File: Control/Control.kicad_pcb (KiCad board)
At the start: 2 copper layers, 157.5 x 90.2 mm, 56 parts, among them J1 Conn_01x04_Pin, J2 Conn_01x08_Pin, J3 Conn_01x08_Pin, J4 Conn_01x07_Pin, SW1 SW_MEC_5E, U1 AT28C64B-15PI, U2 AT28C64B-15PI, U3 SN74AC14N, U4 SN74AC14N, U5 74LS163, U6 74HCT138, U7 74HCT00

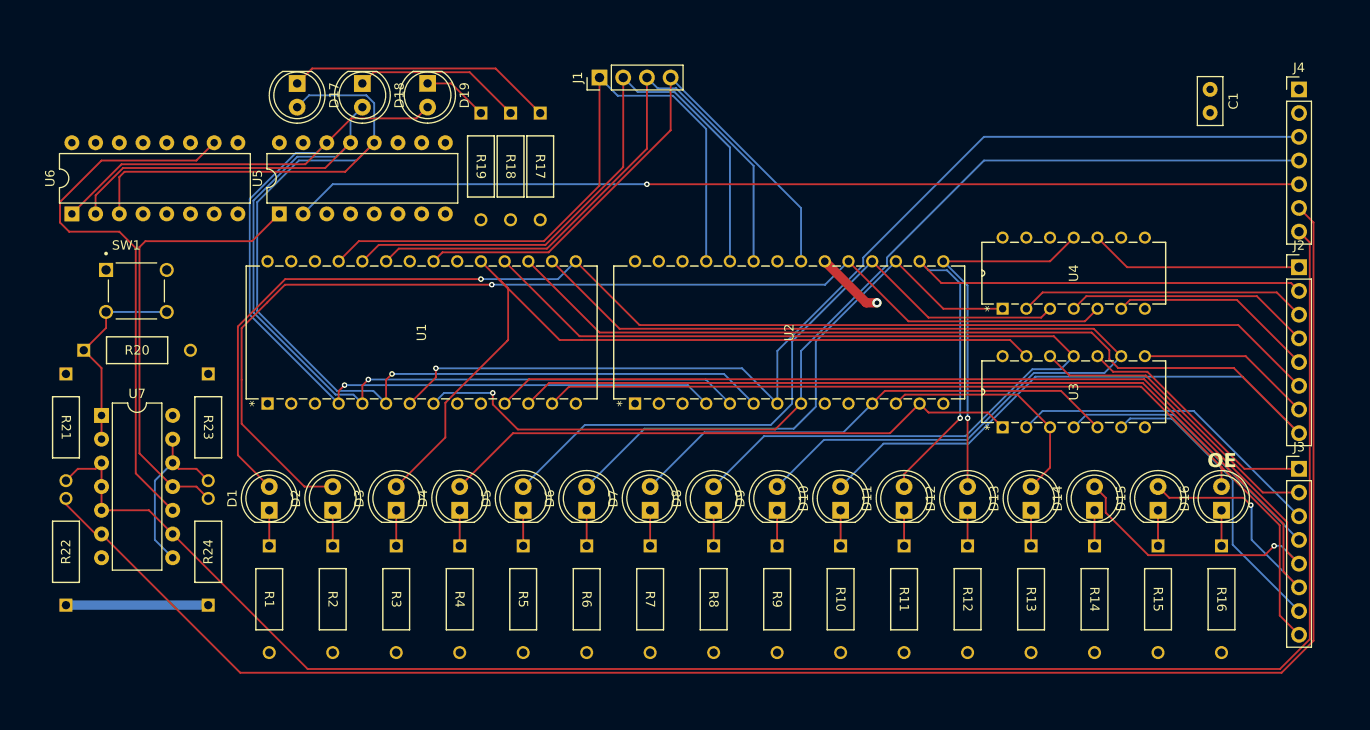
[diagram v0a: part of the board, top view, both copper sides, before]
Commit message: Added silkscreen labels to control LEDs. And other minor silkscreen updates
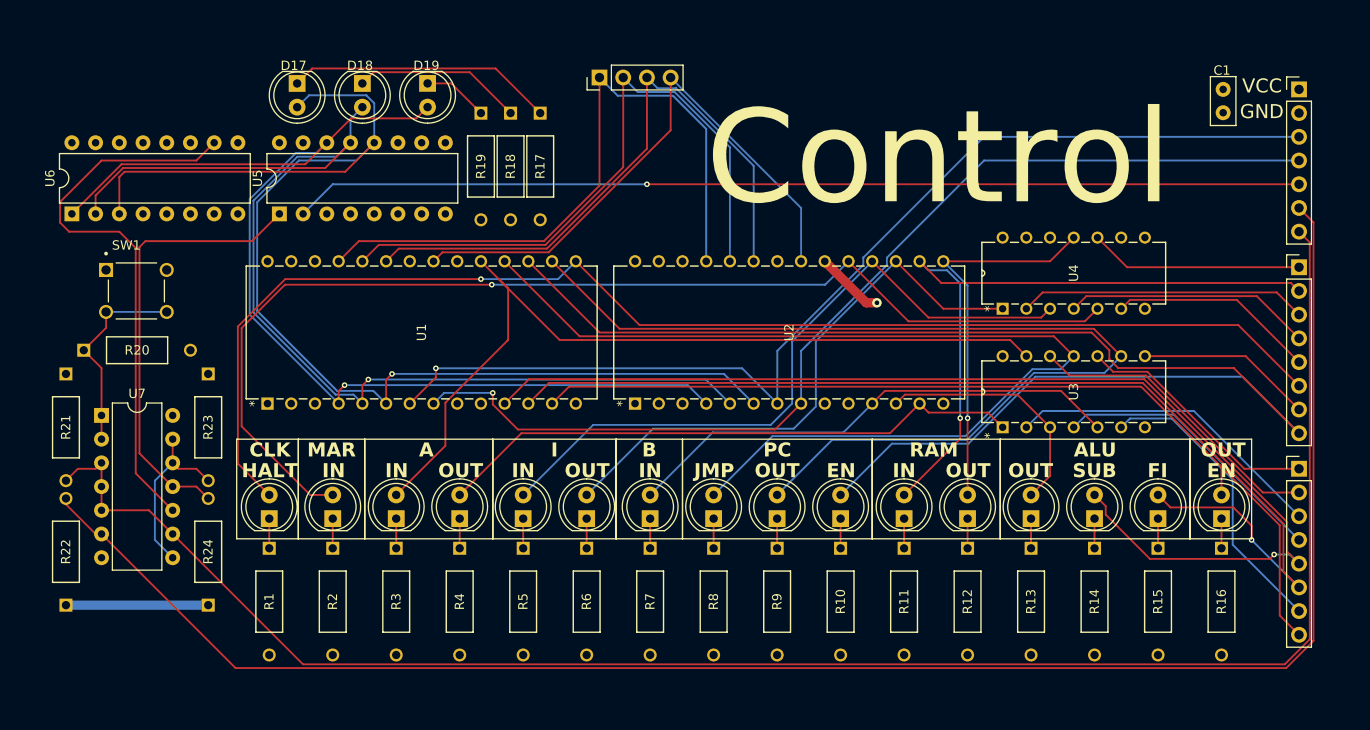
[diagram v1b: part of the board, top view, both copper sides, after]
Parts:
- moved C1 1.40 mm to (182.4, 86.4)
- moved D1 0.89 mm to (80.2, 132.3)
- moved D10 0.89 mm to (141.4, 132.3)
- moved D11 0.89 mm to (148.2, 132.3)
- moved D12 0.89 mm to (155.0, 132.3)
- moved D13 0.89 mm to (161.8, 132.3)
- moved D14 0.89 mm to (168.6, 132.3)
- moved D15 0.89 mm to (175.4, 132.3)
- moved D16 0.89 mm to (182.2, 132.3)
- moved D2 0.89 mm to (87.0, 132.3)
- moved D3 0.89 mm to (93.8, 132.3)
- moved D4 0.89 mm to (100.6, 132.3)
- moved D5 0.89 mm to (107.4, 132.3)
- moved D6 0.89 mm to (114.2, 132.3)
- moved D7 0.89 mm to (121.0, 132.3)
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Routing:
- net /ALU_FLAGS_IN: track 117.3 -> 115.6 mm
- net /ALU_SUB: track 123.3 -> 122.1 mm
- net /Output_EN: track 99.8 -> 100.7 mm
- net /RAM_WO: track 40.2 -> 41.1 mm
- net /RAM_RI: track 71.5 -> 72.4 mm
- net /CLK_Halt: track 140.6 -> 141.5 mm
- net /AR_RI: track 90.2 -> 91.1 mm
- net /ALU_WRITE: track 25.6 -> 26.4 mm
- net Net-(D9-K): track 3.81 -> 3.18 mm
- net Net-(D8-K): track 3.81 -> 3.18 mm
- net Net-(D7-K): track 3.81 -> 3.18 mm
- net Net-(D6-K): track 3.81 -> 3.18 mm
- net Net-(D5-K): track 3.81 -> 3.18 mm
- net Net-(D4-K): track 3.81 -> 3.18 mm
- net Net-(D3-K): track 3.81 -> 3.18 mm
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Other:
- board text added: "A"
- board text added: "ALU"
- board text added: "B"
- board text added: "CLK"
- board text added: "Control"
- board text added: "EN"
- board text added: "FI"
- board text added: "GND"
- board text added: "HALT"
- board text added: "I"
- board text added: "IN"
- board text added: "JMP"
- board text added: "MAR"
- board text added: "OUT"
- board text added: "PC"
- board text added: "RAM"
- board text added: "SUB"
- board text added: "VCC"
- board text removed: "OE"

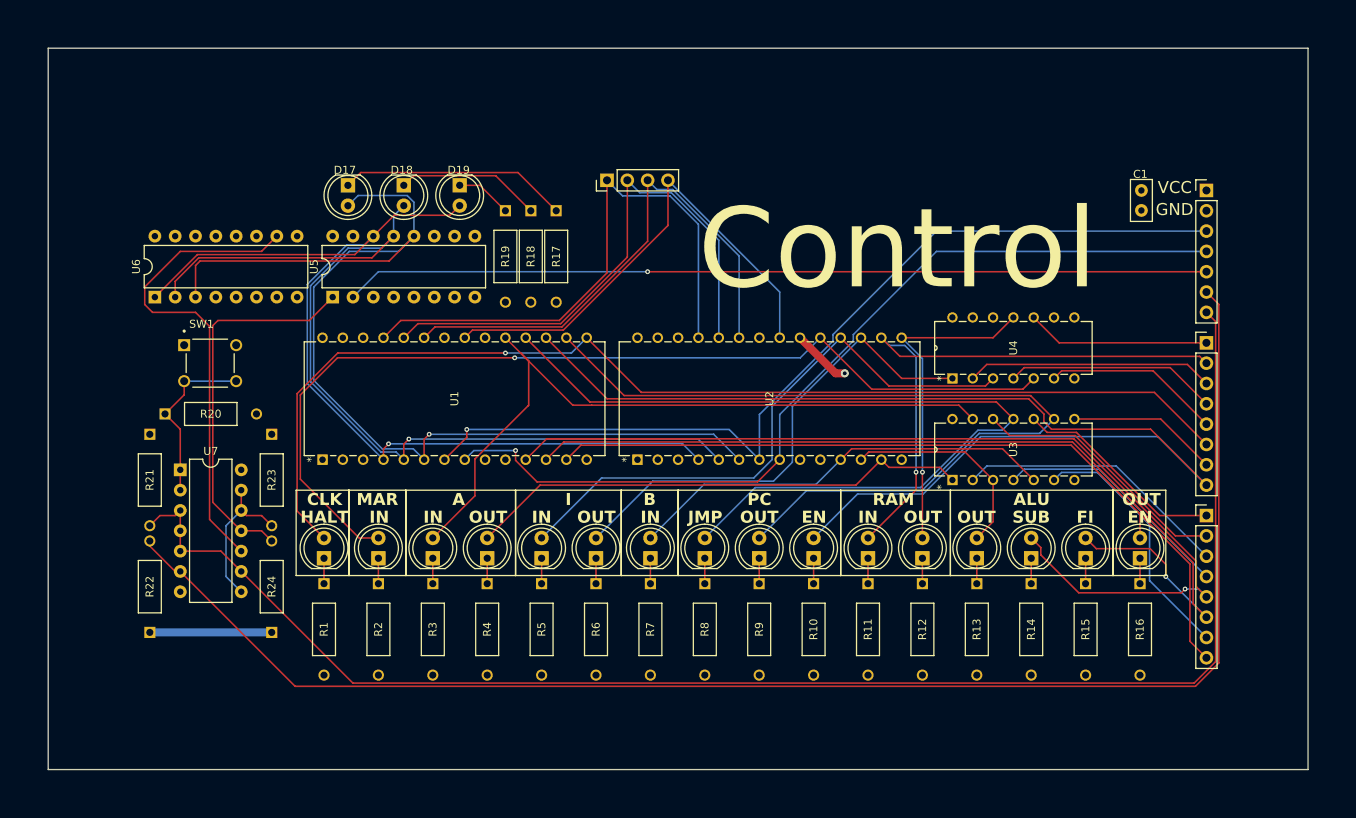
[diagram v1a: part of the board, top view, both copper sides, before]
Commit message: Added edge cuts and mounting holes to control PCB
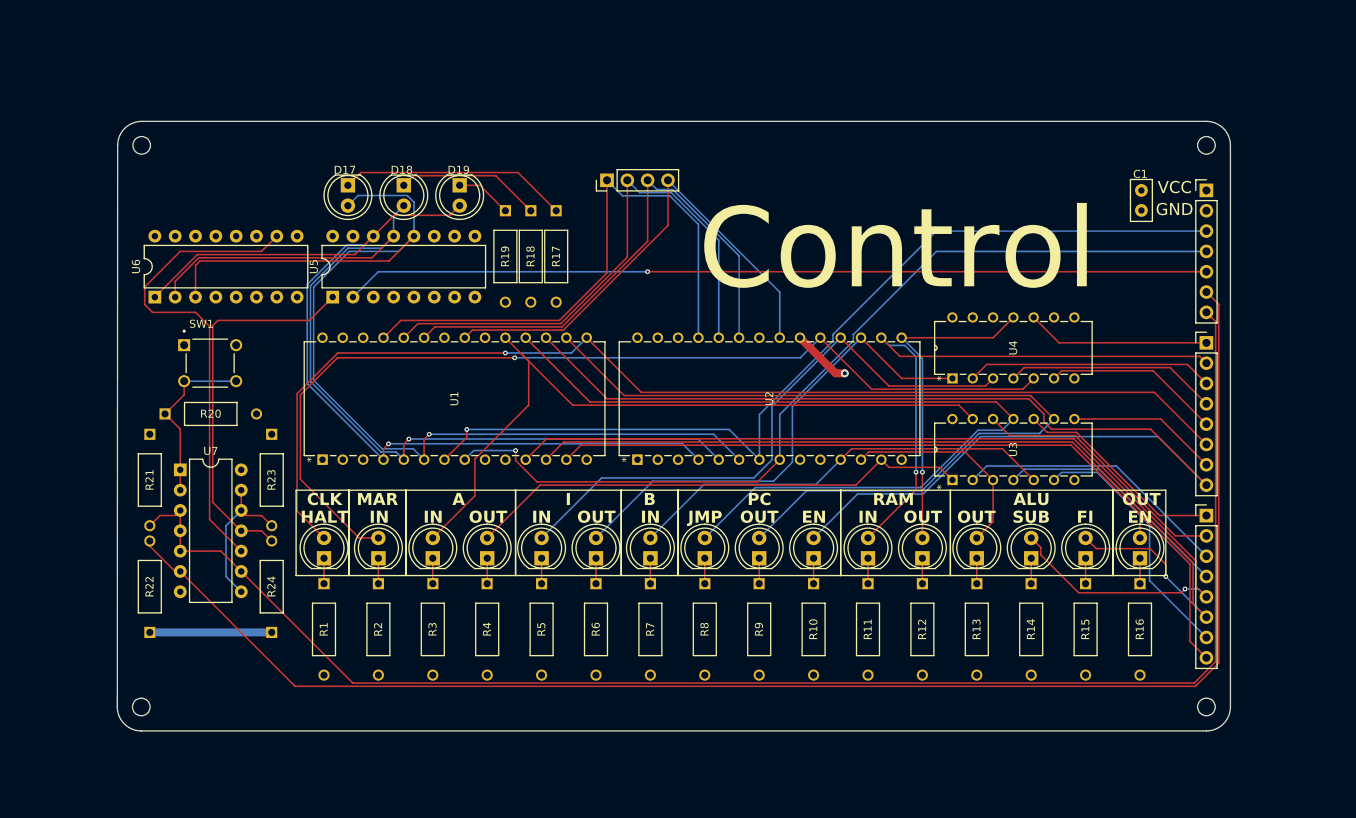
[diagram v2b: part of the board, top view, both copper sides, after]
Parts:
- added REF**: MountingHole_2.2mm_M2, MountingHole:MountingHole_2.2mm_M2, F.Cu at (57.4, 150.9)
- added REF**: MountingHole_2.2mm_M2, MountingHole:MountingHole_2.2mm_M2, F.Cu at (190.5, 80.7)
- added REF**: MountingHole_2.2mm_M2, MountingHole:MountingHole_2.2mm_M2, F.Cu at (190.5, 150.9)
- added REF**: MountingHole_2.2mm_M2, MountingHole:MountingHole_2.2mm_M2, F.Cu at (57.4, 80.7)
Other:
- board size 157.5 x 90.2 mm -> 139.1 x 76.2 mm

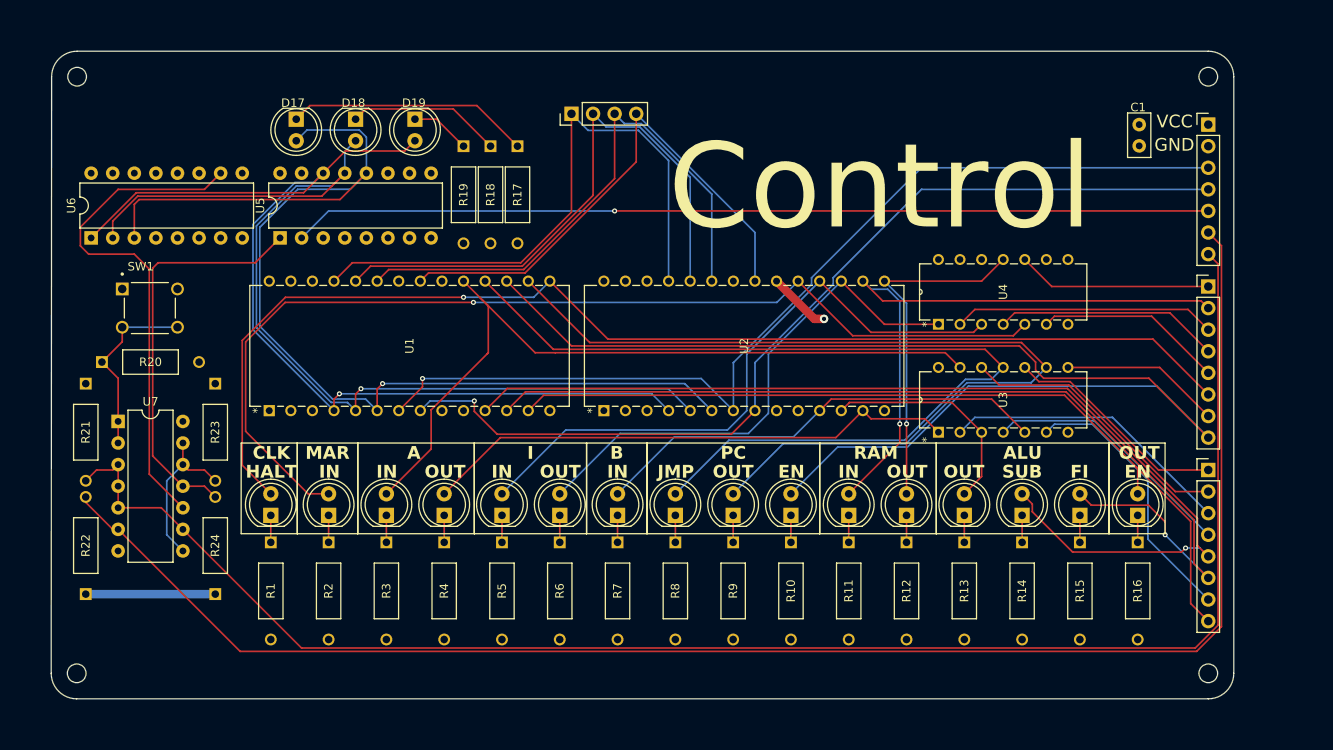
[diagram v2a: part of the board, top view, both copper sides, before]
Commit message: Added silkscrfeen labels to PCB IO pins
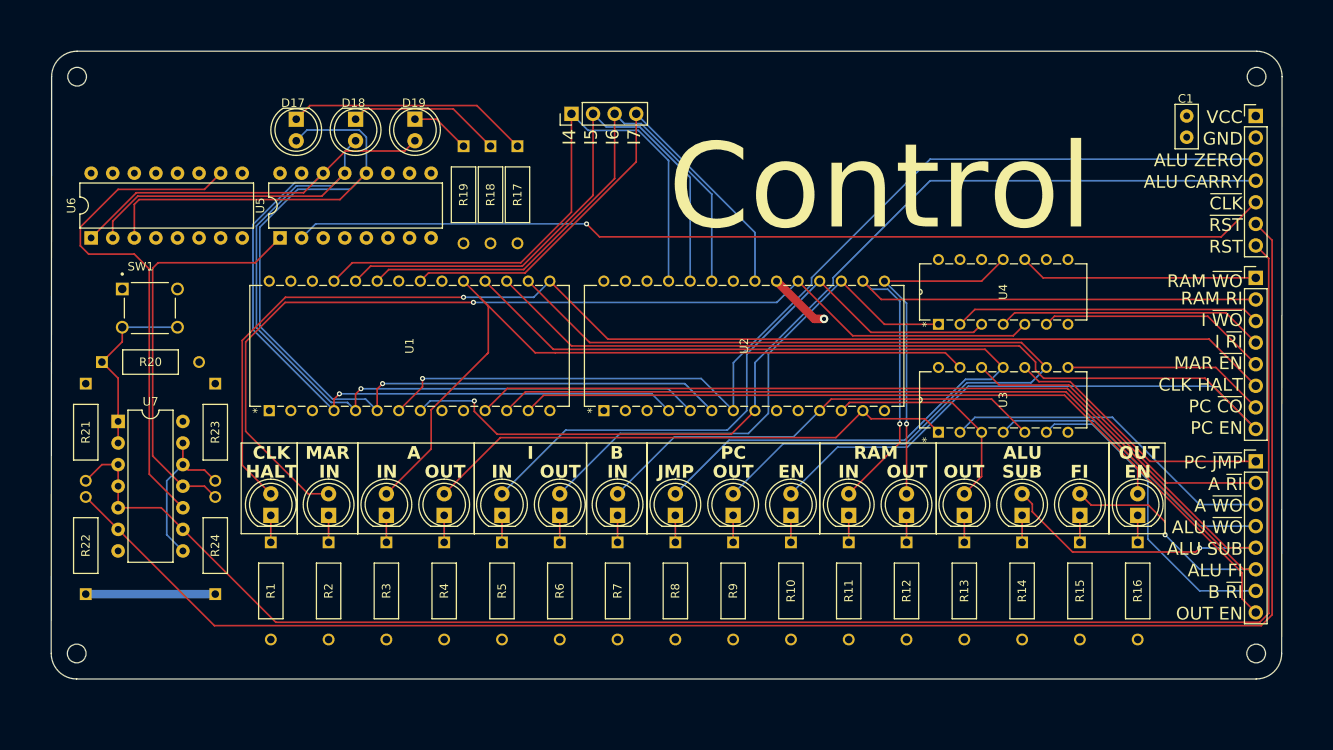
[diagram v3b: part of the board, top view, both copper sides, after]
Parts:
- moved REF** 6.10 mm to (196.1, 148.6)
- moved REF** 5.68 mm to (196.2, 80.7)
- moved C1 5.68 mm to (188.0, 85.3)
- moved J3 5.68 mm to (196.1, 126.0)
- moved J4 5.68 mm to (196.1, 85.3)
- moved J2 5.68 mm to (196.1, 104.4)
- moved REF** 2.33 mm to (57.4, 148.6)
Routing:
- net /PC_CE: track 147.6 -> 157.9 mm
- net /ALU_SUB: track 122.1 -> 130.6 mm
- net /ALU_FLAGS_IN: track 115.6 -> 123.0 mm
- net /~{CLK}: track 108.0 -> 115.3 mm
- net /ALU_ZERO: track 114.6 -> 120.6 mm
- net /ALU_CARRY: track 111.2 -> 117.2 mm
- net /CLK_Halt: track 141.5 -> 146.7 mm
- net /~{MAR_EN}: track 22.2 -> 27.4 mm
- net /~{IR_WO}: track 30.9 -> 36.1 mm
- net /~{AR_RI}: track 32.7 -> 37.9 mm
- net /~{RAM_WO}: track 22.9 -> 28.1 mm
- net /~{PC_JMP}: track 26.6 -> 31.8 mm
- net /~{ALU_WRITE}: track 30.2 -> 35.4 mm
- net /~{PC_CO}: track 18.9 -> 24.0 mm
- net /RAM_RI: track 72.4 -> 77.6 mm
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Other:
- board size 139.1 x 76.2 mm -> 144.8 x 73.9 mm
- board text added: "A ~{RI}"
- board text added: "A ~{WO}"
- board text added: "ALU CARRY"
- board text added: "ALU FI"
- board text added: "ALU SUB"
- board text added: "ALU ZERO"
- board text added: "ALU ~{WO}"
- board text added: "B ~{RI}"
- board text added: "CLK HALT"
- board text added: "I ~{RI}"
- board text added: "I ~{WO}"
- board text added: "I4"
- board text added: "I5"
- board text added: "I6"
- board text added: "I7"
- board text added: "MAR ~{EN}"
- board text added: "OUT EN"
- board text added: "PC EN"
- board text added: "PC ~{CO}"
- board text added: "PC ~{JMP}"
- board text added: "RAM RI"
- board text added: "RAM ~{WO}"
- board text added: "RST"
- board text added: "~{CLK}"
- board text added: "~{RST}"
